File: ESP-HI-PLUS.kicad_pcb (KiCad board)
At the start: 4 copper layers, 58 x 35 mm, 84 parts, among them J1 USB_C_Receptacle_USB2.0_14P, J2 2" IPS LCD, J3 PR5L4015-5P-C-F, J4 PR5L4015-5P-C-F, Q1 AO3401A, Q2 NTK3139P, SW1 SKRPACE010, SW2 SKRPACE010, SW3 JS102011SAQN, U1 MAX40200AUK, U2 ESP32-S3-WROOM-1, U3 TLV75733PDBV, U4 TP4065, U5 DMM-4026-B-I2S-R, U6 MAX40200AUK, U7 MAX98357A, U8 LSM6DSV16X

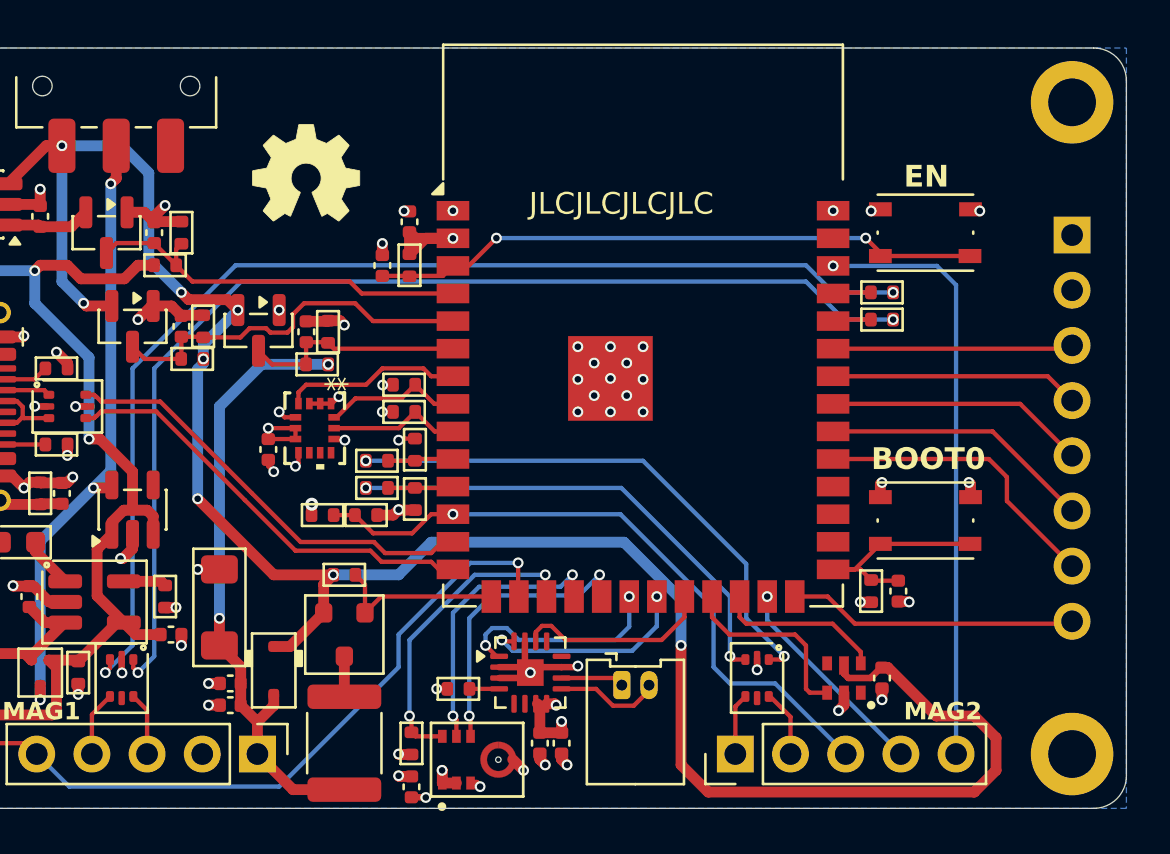
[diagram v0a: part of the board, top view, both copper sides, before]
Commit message: ESP-HI-PLUS v1.1: added microSD card slot and combined I2S in/out ports
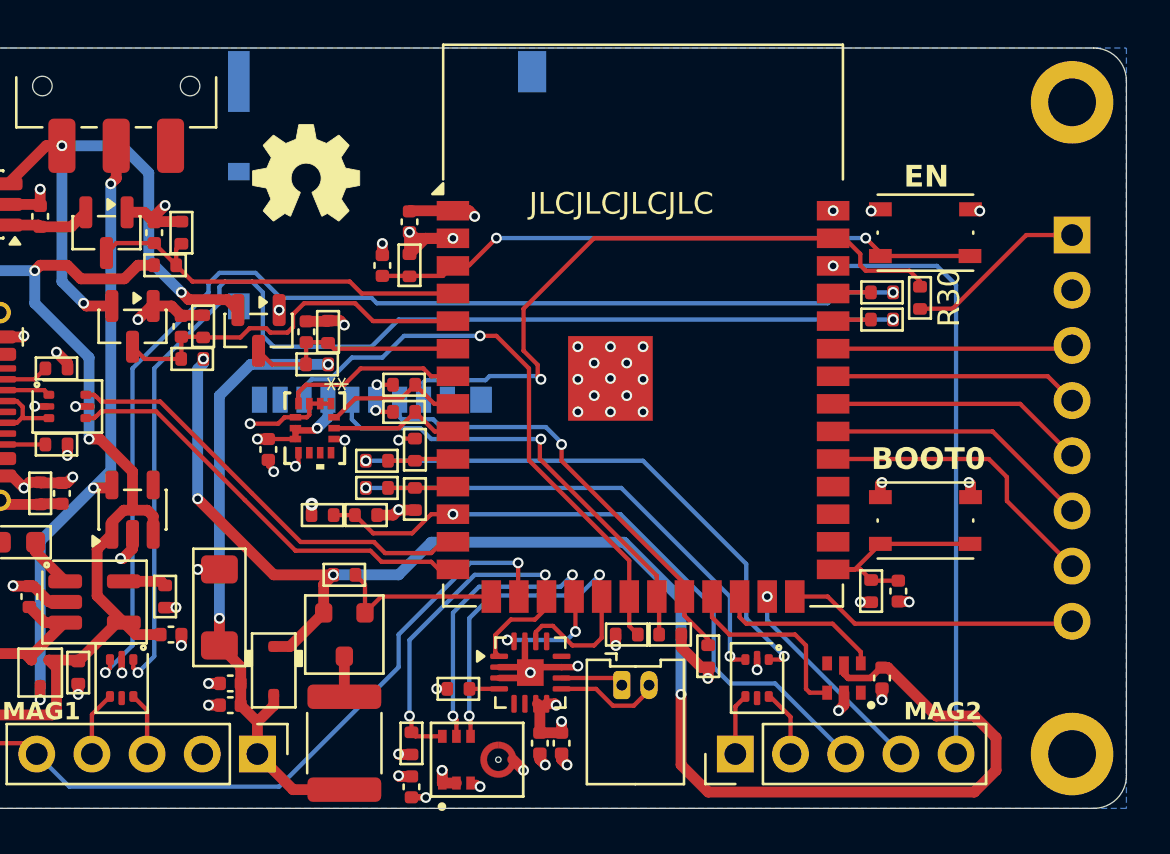
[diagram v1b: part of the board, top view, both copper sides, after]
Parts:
- added J5: Micro_SD_Card, Connector_Card:microSD_HC_Hirose_DM3AT-SF-PEJM5, B.Cu at (134.0, 48.5)
- added R30: 10k, PCM_Resistor_SMD_AKL:R_0402_1005Metric, F.Cu at (158.5, 51.5)
- added R31: 10k, PCM_Resistor_SMD_AKL:R_0402_1005Metric, F.Cu at (148.8, 68.0)
- added R32: 10k, PCM_Resistor_SMD_AKL:R_0402_1005Metric, F.Cu at (145.0, 67.0)
- added R33: 10k, PCM_Resistor_SMD_AKL:R_0402_1005Metric, F.Cu at (147.0, 67.0)
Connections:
- U2 pad 20: /I2S_OUT_DATA -> /SD_MISO
- U2 pad 21: /I2S_OUT_BCLK -> /SD_SCLK
- U2 pad 22: /I2S_OUT_LRCLK -> /SD_MOSI
- U2 pad 39: unconnected-(U2-IO1-Pad39) -> /SD_CS
- U7 pad 1: /I2S_OUT_DATA -> /I2S_IN_DATA
- U7 pad 14: /I2S_OUT_LRCLK -> /I2S_IN_WS
- U7 pad 16: /I2S_OUT_BCLK -> /I2S_IN_BCLK
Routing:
- net /SD_CS: track 0.00 -> 30.9 mm, vias 0 -> 1
- net /SD_MISO: track 0.00 -> 26.9 mm, vias 0 -> 1
- net /SD_SCLK: track 0.00 -> 21.3 mm, vias 0 -> 1
- net /SD_MOSI: track 0.00 -> 20.9 mm, vias 0 -> 1
- net +3V3: track 21.0 -> 35.1 mm, vias 17 -> 19
- net /I2S_OUT_DATA: track 9.94 -> 0.00 mm, vias 2 -> 0
- net /I2S_OUT_BCLK: track 9.77 -> 0.00 mm, vias 2 -> 0
- net /I2S_OUT_LRCLK: track 9.04 -> 0.00 mm
- net /I2S_IN_WS: track 13.3 -> 19.3 mm
- net /I2S_IN_BCLK: track 13.0 -> 18.3 mm, vias 2 -> 4
- net /I2S_IN_DATA: track 14.3 -> 18.7 mm
- net GND: track 50.2 -> 54.4 mm
- net Net-(D7-L1-Pad1): track 51.4 -> 54.0 mm
- net +VSW: track 106.5 -> 107.1 mm, vias 8 -> 7

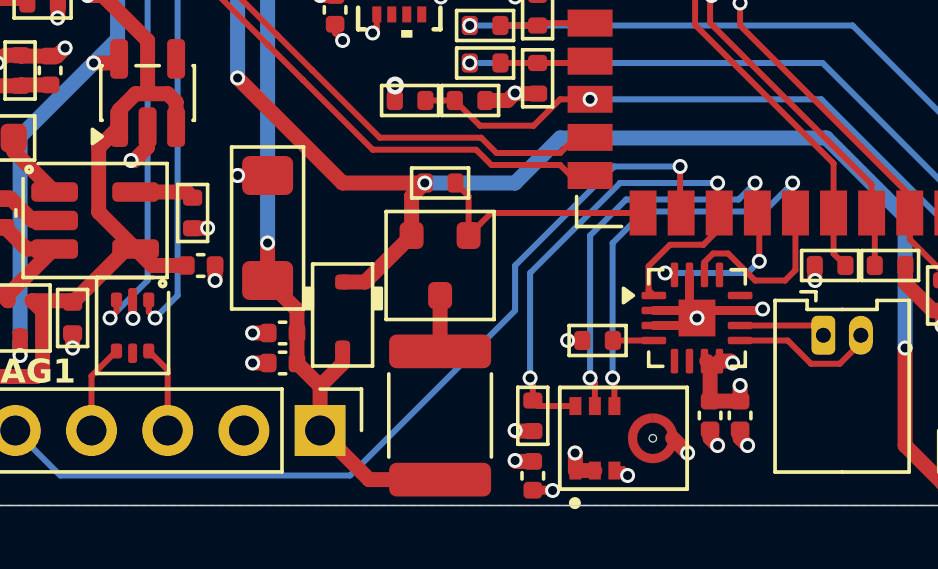
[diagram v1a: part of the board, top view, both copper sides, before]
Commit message: ESP-HI-PLUS v1.15: changed size of 100u capacitor, changed microphone to ICS43434 for availability
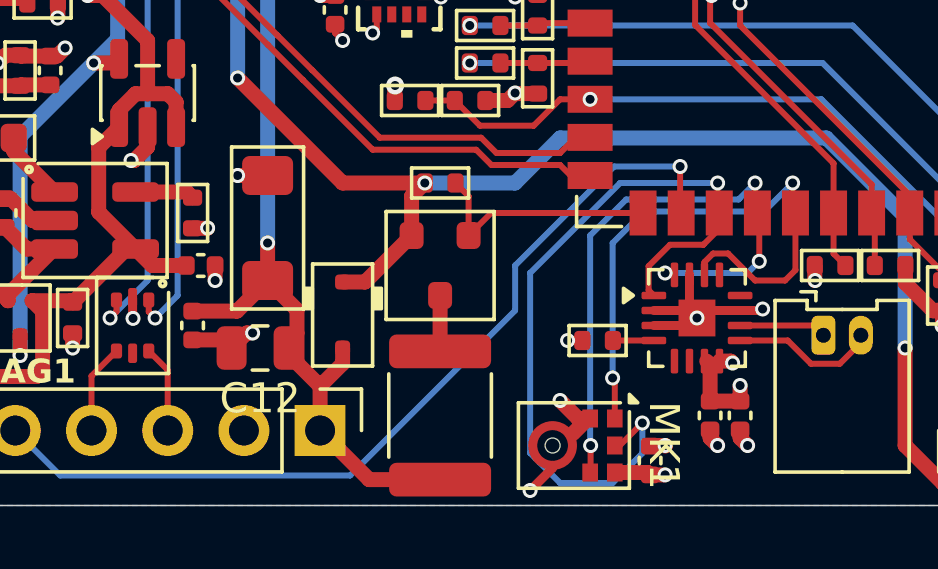
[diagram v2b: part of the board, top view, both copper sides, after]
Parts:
- removed R16: 100k, PCM_Resistor_SMD_AKL:R_0402_1005Metric
- removed U5: DMM-4026-B-I2S-R, MIC_DMM-4026-B-I2S-R:MIC_DMM-4026-B-I2S-R
- added MK1: ICS-43434, Sensor_Audio:InvenSense_ICS-43434-6_3.5x2.65mm, F.Cu at (136.5, 73.0)
- C12: footprint Capacitor_SMD:C_0402_1005Metric -> Capacitor_SMD:C_0805_2012Metric
- moved C9 3.94 mm to (139.0, 73.5)
- moved C11 3.25 mm to (123.8, 69.0), turned to -90 degrees
- moved C12 0.90 mm to (126.0, 69.8)
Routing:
- net /I2S_IN_DATA: track 18.7 -> 25.8 mm
- net VSUB: track 29.1 -> 32.0 mm
- net /I2S_IN_BCLK: track 18.3 -> 20.4 mm
- net GND: track 54.4 -> 56.2 mm, vias 60 -> 58
- net +3V3: track 35.1 -> 35.7 mm, vias 19 -> 18

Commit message: ESP-HI-PLUS v1.15.1: changed VSUB ESD diode
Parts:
- D6: value TGL34-6.8CA -> SMF6.8CA; footprint PCM_Diode_SMD_AKL:D_MiniMELF_TVS -> PCM_Diode_SMD_AKL:D_SOD-123F
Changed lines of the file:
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@@
 		(title "ESP-HI-PLUS")
 		(date "2026-07-20")
-		(rev "v1.1")
+		(rev "v1.15")
 	)
 	(layers
@@
 			)
 		)
-		(property "Description" ""
+		(property "Description" "Resistor, small symbol"
 			(at 0 0 90)
 			(layer "F.Fab")
@@
 			)
 		)
-		(property "Description" ""
+		(property "Description" "Unpolarized capacitor, small symbol"
 			(at 0 0 180)
 			(layer "F.Fab")
@@
 			)
 		)
-		(property "Description" ""
+		(property "Description" "Resistor, small symbol"
 			(at 0 0 90)
 			(layer "F.Fab")
@@
 			)
 		)
-		(property "Datasheet" ""
+		(property "Datasheet" "https://www.invensense.com/wp-content/uploads/2016/02/DS-000069-ICS-43434-v1.2.pdf"
 			(at 0 0 270)
 			(unlocked yes)
@@
 			)
 		)
-		(property "Description" ""
+		(property "Description" "TDK InvenSense MEMS Microphone, 24-bit I2S, 65 dBA SNR, LGA-6"
 			(at 0 0 270)
 			(unlocked yes)
@@
 		)
 	)
-	(footprint "PCM_Diode_SMD_AKL:D_MiniMELF_TVS"
+	(footprint "PCM_Diode_SMD_AKL:D_SOD-123F"
 		(layer "F.Cu")
 		(at 126.25 65.75 -90)
-		(descr "Diode Mini-MELF, Bidirectional zener or TVS, Alternate KiCad Library")
-		(tags "Diode Mini-MELF TVS")
+		(descr "D_SOD-123F, Alternate KiCad Library")
+		(tags "D_SOD-123F")
 		(property "Reference" "D6"
-			(at 0 -2.127 90)
+			(at 0 -2.159 270)
 			(layer "F.SilkS")
 			(hide yes)
@@
 			)
 		)
-		(property "Value" "TGL34-6.8CA"
-			(at 0 1.75 90)
+		(property "Value" "SMF6.8CA"
+			(at 0 2.1 270)
 			(layer "F.Fab")
 			(hide yes)
@@
 		)
 		(property "Datasheet" "https://www.tme.eu/Document/9bde1516908ec192c3b5a07e8cc13ddb/tgl3468.pdf"
-			(at 0 0 90)
+			(at 0 0 270)
 			(layer "F.Fab")
 			(hide yes)
@@
 		)
 		(property "Description" "MiniMELF Bidirectional TVS Diode, 6.8V, 150W, Alternate KiCAD Library"
-			(at 0 0 90)
+			(at 0 0 270)
 			(layer "F.Fab")
 			(hide yes)
@@
 		(duplicate_pad_numbers_are_jumpers no)
 		(fp_line
-			(start -2.7 1.2)
-			(end 2.7 1.2)
+			(start -2.3 1.2)
+			(end 2.3 1.2)
 			(stroke
 				(width 0.12)
@@
 		)
 		(fp_line
-			(start 2.7 1.2)
-			(end 2.7 -1.2)
+			(start 2.3 1.2)
+			(end 2.3 -1.2)
 			(stroke
 				(width 0.12)
@@
 		)
 		(fp_line
-			(start -2.7 -1.2)
-			(end -2.7 1.2)
+			(start -2.3 -1.2)
+			(end -2.3 1.2)
 			(stroke
 				(width 0.12)
@@
 		)
 		(fp_line
-			(start 2.7 -1.2)
-			(end -2.7 -1.2)
+			(start 2.3 -1.2)
+			(end -2.3 -1.2)
 			(stroke
 				(width 0.12)
@@
 			(layer "F.SilkS")
 		)
+		(fp_poly
+			(pts
+				(xy -0.6 1.5) (xy -1.4 1.5) (xy -1.4 1.2) (xy -0.6 1.2)
+			)
+			(stroke
+				(width 0.1)
+				(type solid)
+			)
+			(fill yes)
+			(layer "F.SilkS")
+		)
+		(fp_poly
+			(pts
+				(xy -0.6 -1.2) (xy -1.4 -1.2) (xy -1.4 -1.5) (xy -0.6 -1.5)
+			)
+			(stroke
+				(width 0.1)
+				(type solid)
+			)
+			(fill yes)
+			(layer "F.SilkS")
+		)
 		(fp_line
-			(start -2.65 1.1)
-			(end -2.65 -1.1)
+			(start 2.2 1.15)
+			(end -2.2 1.15)
 			(stroke
 				(width 0.05)
@@
 		)
 		(fp_line
-			(start 2.65 1.1)
-			(end -2.65 1.1)
+			(start -2.2 -1.15)
+			(end -2.2 1.15)
 			(stroke
 				(width 0.05)
@@
 		)
 		(fp_line
-			(start -2.65 -1.1)
-			(end 2.65 -1.1)
+			(start -2.2 -1.15)
+			(end 2.2 -1.15)
 			(stroke
 				(width 0.05)
@@
 		)
 		(fp_line
-			(start 2.65 -1.1)
-			(end 2.65 1.1)
+			(start 2.2 -1.15)
+			(end 2.2 1.15)
 			(stroke
 				(width 0.05)
@@
 		)
 		(fp_line
-			(start -1.65 0.8)
-			(end -1.65 -0.8)
+			(start -1.4 0.9)
+			(end -1.4 -0.9)
+			(stroke
+				(width 0.1)
+				(type solid)
+			)
+			(layer "F.Fab")
+		)
+		(fp_line
+			(start 1.4 0.9)
+			(end -1.4 0.9)
+			(stroke
+				(width 0.1)
+				(type solid)
+			)
+			(layer "F.Fab")
+		)
+		(fp_line
+			(start -1.85 0.35)
+			(end -1.4 0.35)
+			(stroke
+				(width 0.1)
+				(type solid)
+			)
+			(layer "F.Fab")
+		)
+		(fp_line
+			(start 1.85 0.35)
+			(end 1.4 0.35)
+			(stroke
+				(width 0.1)
+				(type solid)
+			)
+			(layer "F.Fab")
+		)
+		(fp_line
+			(start 1.85 0.35)
+			(end 1.85 -0.35)
 			(stroke
 				(width 0.1)
@@
 		)
 		(fp_line
-			(start 1.65 0.8)
-			(end -1.65 0.8)
+			(start -1.85 -0.35)
+			(end -1.85 0.35)
 			(stroke
 				(width 0.1)
@@
 		)
 		(fp_line
-			(start -1.65 -0.8)
-			(end 1.65 -0.8)
+			(start -1.85 -0.35)
+			(end -1.4 -0.35)
 			(stroke
 				(width 0.1)
@@
 		)
 		(fp_line
-			(start -1.1 -0.8)
-			(end -1.1 0.8)
+			(start 1.85 -0.35)
+			(end 1.4 -0.35)
 			(stroke
 				(width 0.1)
@@
 		)
 		(fp_line
-			(start 1.1 -0.8)
-			(end 1.1 0.8)
+			(start -1.4 -0.9)
+			(end 1.4 -0.9)
 			(stroke
 				(width 0.1)
@@
 		)
 		(fp_line
-			(start 1.65 -0.8)
-			(end 1.65 0.8)
+			(start 1.4 -0.9)
+			(end 1.4 0.9)
 			(stroke
 				(width 0.1)
@@
 			(layer "F.Fab")
 		)
+		(fp_rect
+			(start -1 -0.9)
+			(end -0.6 0.9)
+			(stroke
+				(width 0.1)
+				(type solid)
+			)
+			(fill yes)
+			(layer "F.Fab")
+		)
 		(fp_text user "${REFERENCE}"
-			(at 0 0 90)
+			(at 0.4 0 270)
 			(layer "F.Fab")
 			(effects
@@
 		)
 		(pad "1" smd roundrect
-			(at -1.75 0 270)
-			(size 1.3 1.7)
+			(at -1.4 0 270)
+			(size 1.1 1.1)
 			(layers "F.Cu" "F.Mask" "F.Paste")
-			(roundrect_rratio 0.1923076923)
+			(roundrect_rratio 0.2272727273)
 			(net "GND")
 			(pinfunction "K_1")
@@
 		)
 		(pad "2" smd roundrect
-			(at 1.75 0 270)
-			(size 1.3 1.7)
+			(at 1.4 0 270)
+			(size 1.1 1.1)
 			(layers "F.Cu" "F.Mask" "F.Paste")
-			(roundrect_rratio 0.1923076923)
+			(roundrect_rratio 0.2272727273)
 			(net "VSUB")
 			(pinfunction "A_2")
@@
 		)
 		(embedded_fonts no)
-		(model "${KICAD10_3DMODEL_DIR}/Diode_SMD.3dshapes/D_MiniMELF.step"
+		(model "${KICAD6_3DMODEL_DIR}/Diode_SMD.3dshapes/D_SOD-123F.wrl"
 			(offset
 				(xyz 0 0 0)
@@
 			)
 		)
-		(property "Description" ""
+		(property "Description" "Resistor, small symbol"
 			(at 0 0 0)
 			(layer "F.Fab")
@@
 			)
 		)
-		(property "Description" ""
+		(property "Description" "Resistor, small symbol"
 			(at 0 0 0)
 			(layer "F.Fab")
@@
 			)
 		)
-		(property "Datasheet" ""
+		(property "Datasheet" "https://www.we-online.com/components/products/datasheet/693072010801.pdf"
 			(at 0 0 180)
 			(unlocked yes)
@@
 			)
 		)
-		(property "Description" ""
+		(property "Description" "Micro SD Card Socket"
 			(at 0 0 180)
 			(unlocked yes)

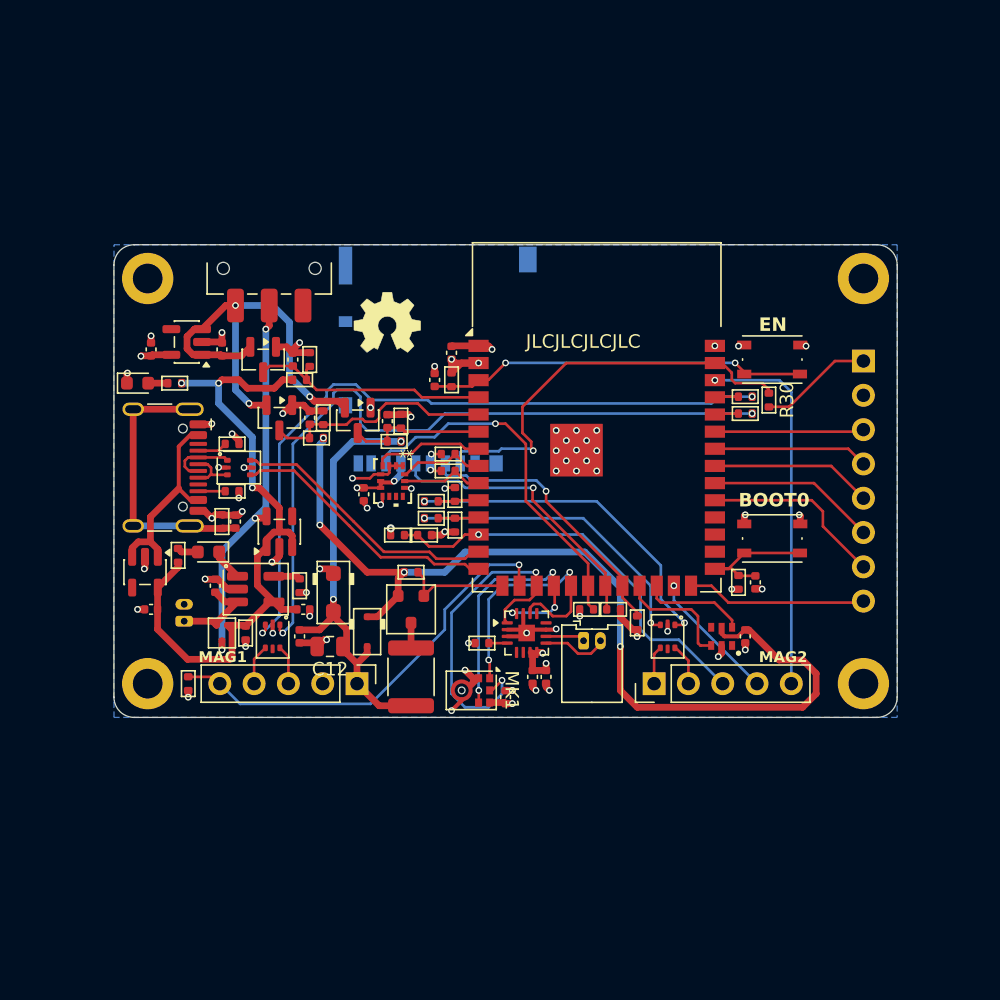
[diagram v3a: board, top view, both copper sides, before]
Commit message: add 70x70 board edge for PCB manufacturing
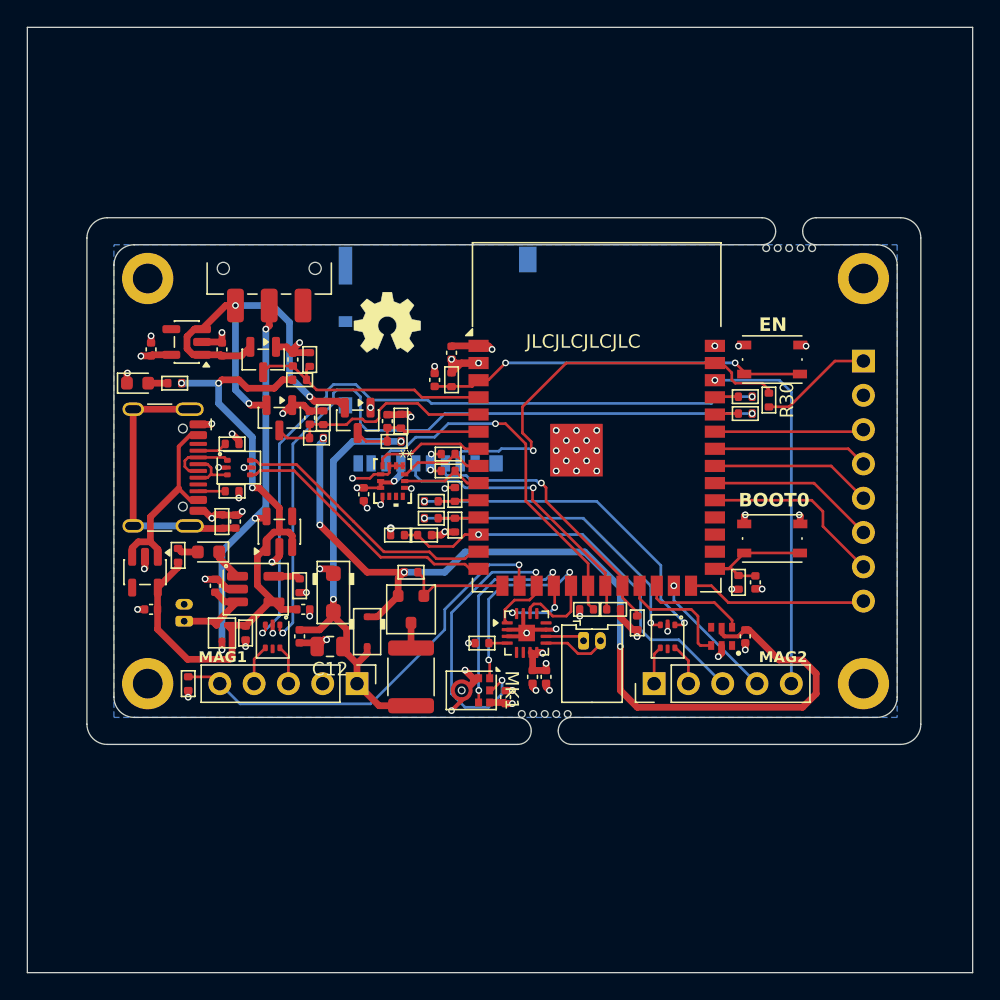
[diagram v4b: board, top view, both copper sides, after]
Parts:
- added REF**: MouseBite-Part_2.0x2.0mm_inset_D0.5mm_P0.85mm_5h, Panelization:MouseBite-Part_2.0x2.0mm_inset_D0.5mm_P0.85mm_5h, F.Cu at (141.9, 75.0)
- added REF**: MouseBite-Part_2.0x2.0mm_inset_D0.5mm_P0.85mm_5h, Panelization:MouseBite-Part_2.0x2.0mm_inset_D0.5mm_P0.85mm_5h, F.Cu at (160.0, 40.0)
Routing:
- net +3V3: track 35.7 -> 36.9 mm
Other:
- board size 58 x 35 mm -> 70 x 70 mm

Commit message: minor fixes
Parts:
- removed REF** (x2): MouseBite-Part_2.0x2.0mm_inset_D0.5mm_P0.85mm_5h, Panelization:MouseBite-Part_2.0x2.0mm_inset_D0.5mm_P0.85mm_5h
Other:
- board size 70 x 70 mm -> 58 x 35 mm

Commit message: ESP-HI-PLUS v1.17: Changed RGB LED to 2020 NeoPixel
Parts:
- removed D3: SK9822-EC20, PCM_SparkFun-LED:APA102_2020-6Pin
- removed U4: TP4065, PCM_Package_TO_SOT_SMD_AKL:SOT-23-5_BigPads
- added D12: WS2812B-2020, LED_SMD:LED_WS2812B-2020_PLCC4_2.0x2.0mm, F.Cu at (155.0, 69.0)
- added U5: TP4065, Package_TO_SOT_SMD:SOT-23-5_HandSoldering, F.Cu at (120.5, 65.5)
- turned C8 to 90 degrees
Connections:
- U2 pad 24: /RGB_CLK -> unconnected-(U2-IO47-Pad24)
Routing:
- net /RGB_CLK: track 7.71 -> 0.00 mm
- net +VSW: track 107.1 -> 105.4 mm
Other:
- board text added: "+"
- board text added: "SPK"
